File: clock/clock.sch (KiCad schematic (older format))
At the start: 3 parts, among them P101 CONN_01X03, P102 CONN_FAN_PWM, P103 XG4A-1631

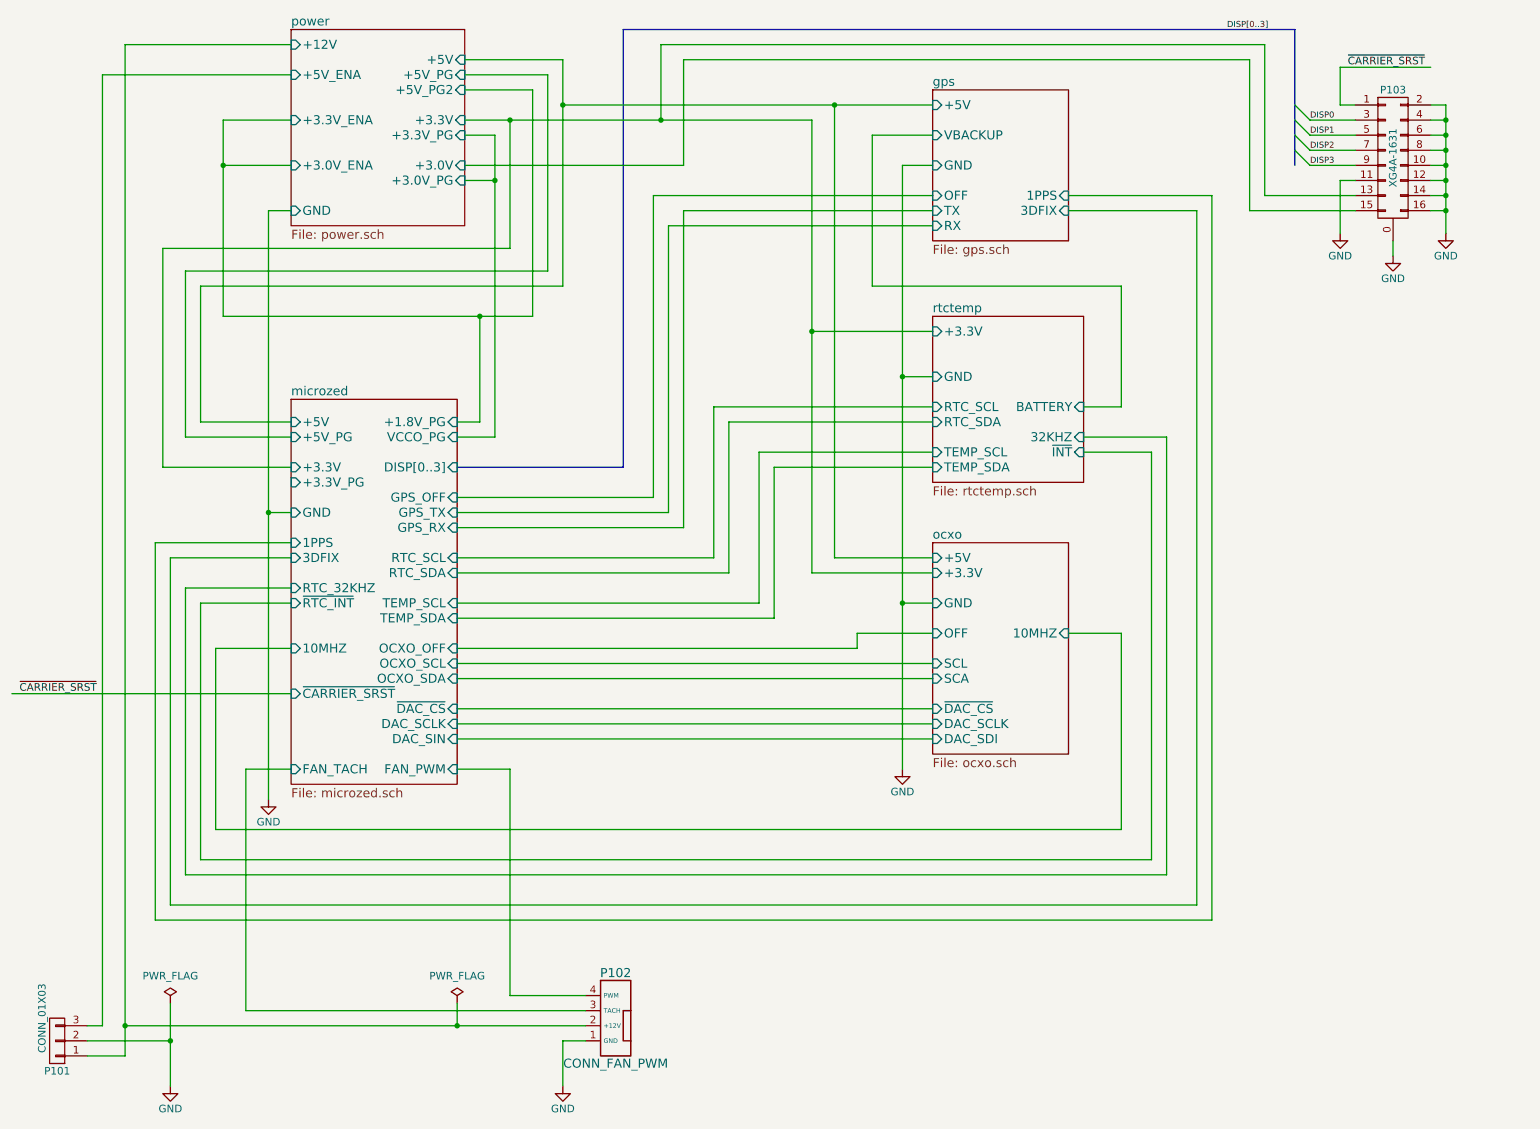
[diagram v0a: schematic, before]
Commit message: Start next revision of the main board. Power sequencing and control changes.
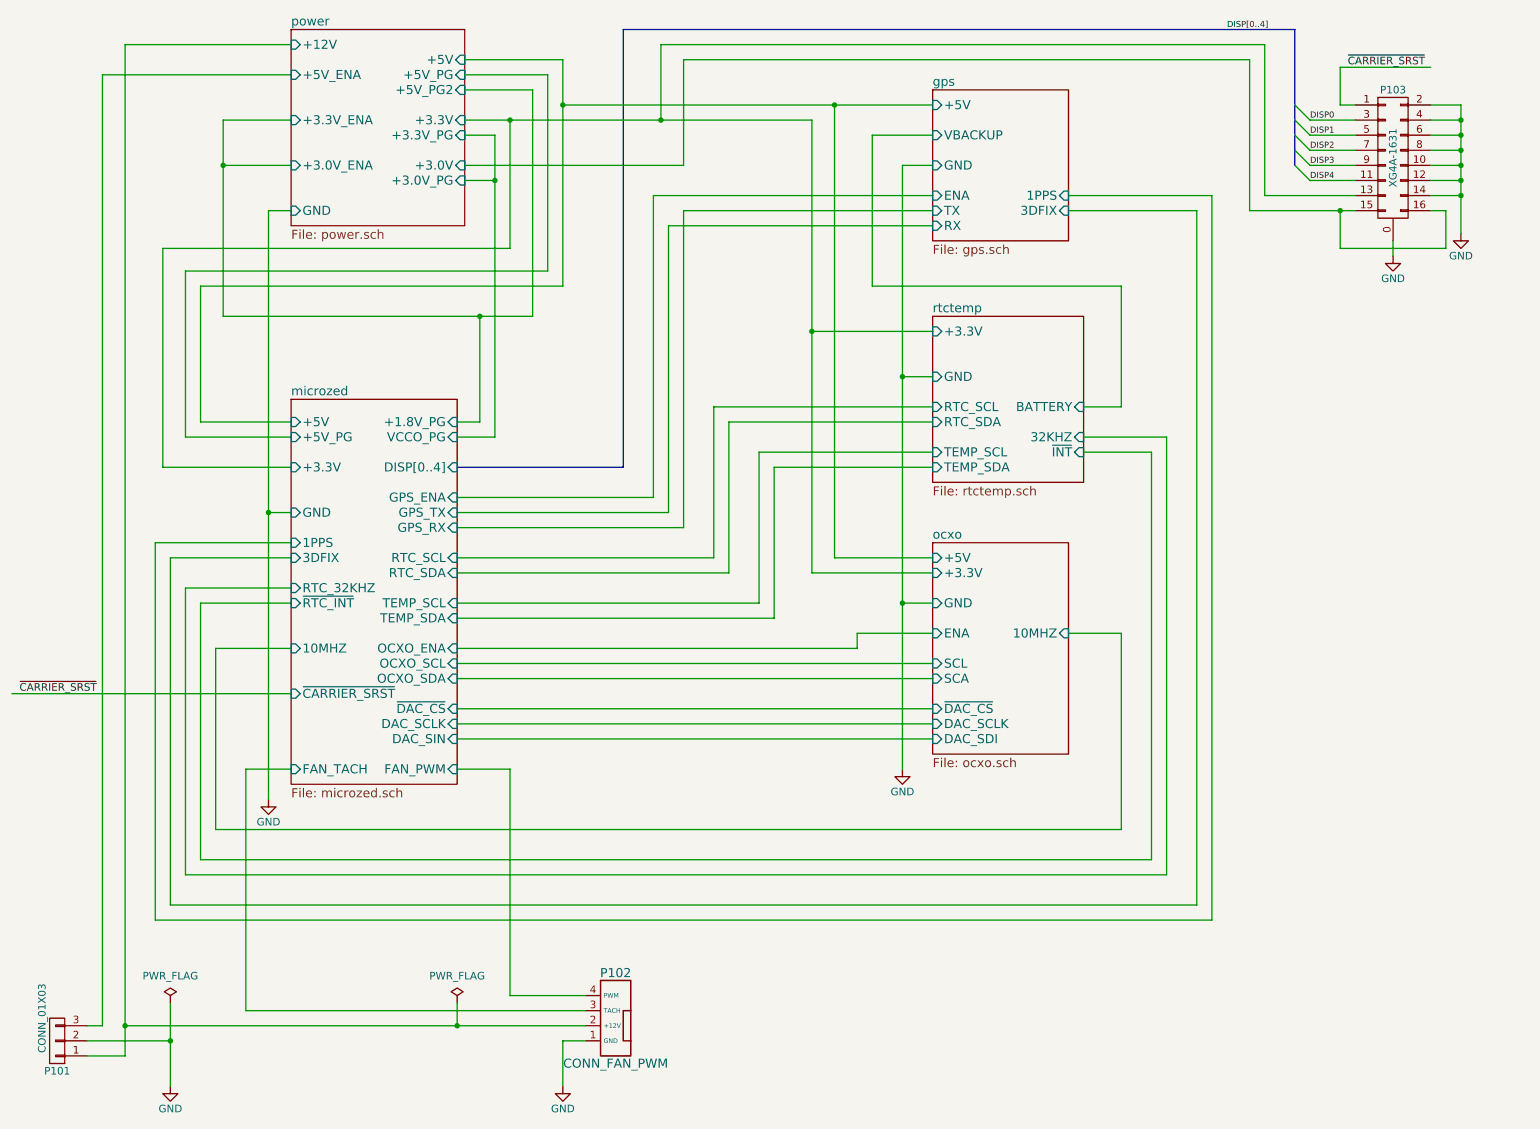
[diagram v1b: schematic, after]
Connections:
- net GND: no longer P103.11 (P11), P103.16 (P16)
- net power/+3.0V: now also P103.16 (P16)
- new net DISP4: P103.11 (P11)
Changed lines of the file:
@@
 F9 "DAC_SDI" I L 6650 5300 60
 F10 "+3.3V" I L 6650 4200 60
-F11 "OFF" I L 6650 4600 60
+F11 "ENA" I L 6650 4600 60
 $EndSheet
 $Sheet
@@
 F7 "VBACKUP" I L 6650 1300 60
 F8 "GND" I L 6650 1500 60
-F9 "OFF" I L 6650 1700 60
+F9 "ENA" I L 6650 1700 60
 $EndSheet
 $Sheet
@@
 F4 "GND" I L 2400 3800 60
 F5 "+5V_PG" I L 2400 3300 60
-F6 "+3.3V_PG" I L 2400 3600 60
-F7 "+1.8V_PG" I R 3500 3200 60
-F8 "VCCO_PG" I R 3500 3300 60
-F9 "GPS_TX" I R 3500 3800 60
-F10 "GPS_RX" I R 3500 3900 60
-F11 "OCXO_SCL" I R 3500 4800 60
-F12 "OCXO_SDA" I R 3500 4900 60
-F13 "~DAC_CS~" I R 3500 5100 60
-F14 "DAC_SCLK" I R 3500 5200 60
-F15 "DAC_SIN" I R 3500 5300 60
-F16 "10MHZ" I L 2400 4700 60
-F17 "1PPS" I L 2400 4000 60
-F18 "3DFIX" I L 2400 4100 60
-F19 "FAN_PWM" I R 3500 5500 60
-F20 "DISP[0..3]" I R 3500 3500 60
-F21 "RTC_SCL" I R 3500 4100 60
-F22 "RTC_SDA" I R 3500 4200 60
-F23 "TEMP_SCL" I R 3500 4400 60
-F24 "TEMP_SDA" I R 3500 4500 60
-F25 "FAN_TACH" I L 2400 5500 60
-F26 "~CARRIER_SRST~" I L 2400 5000 60
-F27 "GPS_OFF" I R 3500 3700 60
-F28 "OCXO_OFF" I R 3500 4700 60
-F29 "RTC_32KHZ" I L 2400 4300 60
-F30 "~RTC_INT~" I L 2400 4400 60
+F6 "+1.8V_PG" I R 3500 3200 60
+F7 "VCCO_PG" I R 3500 3300 60
+F8 "GPS_TX" I R 3500 3800 60
+F9 "GPS_RX" I R 3500 3900 60
+F10 "OCXO_SCL" I R 3500 4800 60
+F11 "OCXO_SDA" I R 3500 4900 60
+F12 "~DAC_CS~" I R 3500 5100 60
+F13 "DAC_SCLK" I R 3500 5200 60
+F14 "DAC_SIN" I R 3500 5300 60
+F15 "10MHZ" I L 2400 4700 60
+F16 "1PPS" I L 2400 4000 60
+F17 "3DFIX" I L 2400 4100 60
+F18 "FAN_PWM" I R 3500 5500 60
+F19 "DISP[0..4]" I R 3500 3500 60
+F20 "RTC_SCL" I R 3500 4100 60
+F21 "RTC_SDA" I R 3500 4200 60
+F22 "TEMP_SCL" I R 3500 4400 60
+F23 "TEMP_SDA" I R 3500 4500 60
+F24 "FAN_TACH" I L 2400 5500 60
+F25 "~CARRIER_SRST~" I L 2400 5000 60
+F26 "GPS_ENA" I R 3500 3700 60
+F27 "OCXO_ENA" I R 3500 4700 60
+F28 "RTC_32KHZ" I L 2400 4300 60
+F29 "~RTC_INT~" I L 2400 4400 60
 $EndSheet
 $Comp
@@
 L GND #PWR03
 U 1 1 5632D32A
-P 10050 1950
-F 0 "#PWR03" H 10050 1700 50  0001 C CNN
-F 1 "GND" H 10050 1800 50  0000 C CNN
-F 2 "" H 10050 1950 60  0000 C CNN
-F 3 "" H 10050 1950 60  0000 C CNN
-	1    10050 1950
-	1    0    0    -1
-$EndComp
-$Comp
-L GND #PWR04
-U 1 1 5632E81A
-P 9350 1950
-F 0 "#PWR04" H 9350 1700 50  0001 C CNN
-F 1 "GND" H 9350 1800 50  0000 C CNN
-F 2 "" H 9350 1950 60  0000 C CNN
-F 3 "" H 9350 1950 60  0000 C CNN
-	1    9350 1950
+P 10150 1950
+F 0 "#PWR03" H 10150 1700 50  0001 C CNN
+F 1 "GND" H 10150 1800 50  0000 C CNN
+F 2 "" H 10150 1950 60  0000 C CNN
+F 3 "" H 10150 1950 60  0000 C CNN
+	1    10150 1950
 	1    0    0    -1
 $EndComp
@@
 DISP3
 Text Label 8600 600  0    40   ~ 0
-DISP[0..3]
+DISP[0..4]
 $Comp
 L CONN_FAN_PWM P102
@@
 	1700 3300 2400 3300
 Wire Wire Line
-	10050 1800 9950 1800
-Connection ~ 10050 1800
-Wire Wire Line
-	10050 1700 9950 1700
-Connection ~ 10050 1700
-Wire Wire Line
-	10050 1600 9950 1600
-Connection ~ 10050 1600
-Wire Wire Line
-	10050 1500 9950 1500
-Connection ~ 10050 1500
-Wire Wire Line
-	10050 1400 9950 1400
-Connection ~ 10050 1400
-Wire Wire Line
-	10050 1300 9950 1300
-Connection ~ 10050 1300
-Wire Wire Line
-	9950 1200 10050 1200
+	10150 1700 9950 1700
+Connection ~ 10150 1700
+Wire Wire Line
+	10150 1600 9950 1600
+Connection ~ 10150 1600
+Wire Wire Line
+	10150 1500 9950 1500
+Connection ~ 10150 1500
+Wire Wire Line
+	10150 1400 9950 1400
+Connection ~ 10150 1400
+Wire Wire Line
+	10150 1300 9950 1300
+Connection ~ 10150 1300
+Wire Wire Line
+	9950 1200 10150 1200
 Wire Wire Line
 	9450 1100 9350 1100
-Wire Wire Line
-	9450 1600 9350 1600
 Wire Wire Line
 	3550 1500 5000 1500
@@
 ~CARRIER_SRST~
 Wire Wire Line
-	10050 1100 10050 1950
+	10150 1100 10150 1950
 Wire Wire Line
 	9350 850  9950 850
@@
 	9350 1100 9350 850
 Wire Wire Line
-	9950 1100 10050 1100
-Connection ~ 10050 1200
-Wire Wire Line
-	9350 1600 9350 1950
+	9950 1100 10150 1100
+Connection ~ 10150 1200
 Wire Wire Line
 	3550 1000 4000 1000
@@
 Wire Wire Line
 	4900 1900 4900 3800
+Entry Wire Line
+	9050 1500 9150 1600
+Wire Wire Line
+	9150 1600 9450 1600
+Text Label 9150 1600 0    40   ~ 0
+DISP4
+Wire Wire Line
+	9950 1800 10050 1800
+Wire Wire Line
+	10050 1800 10050 2050
+Wire Wire Line
+	10050 2050 9350 2050
+Wire Wire Line
+	9350 2050 9350 1800
+Connection ~ 9350 1800
 $EndSCHEMATC

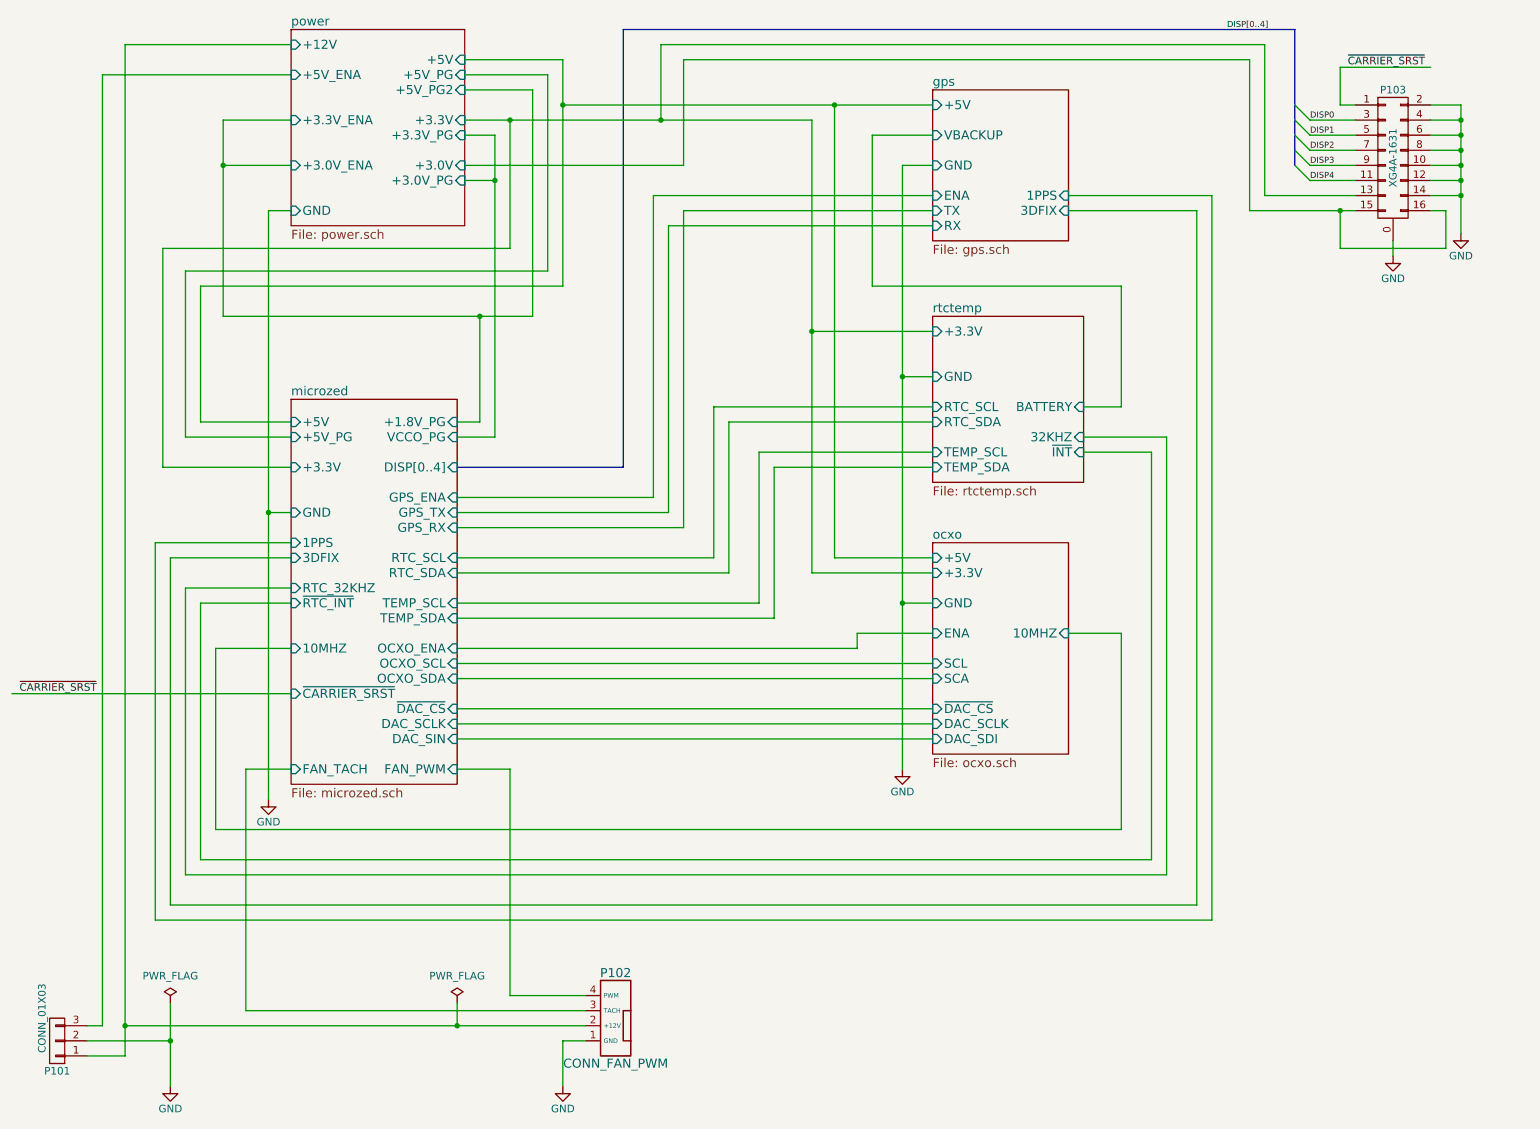
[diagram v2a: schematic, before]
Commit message: Remove sheet to sheet power interconnect because power symbols are global.
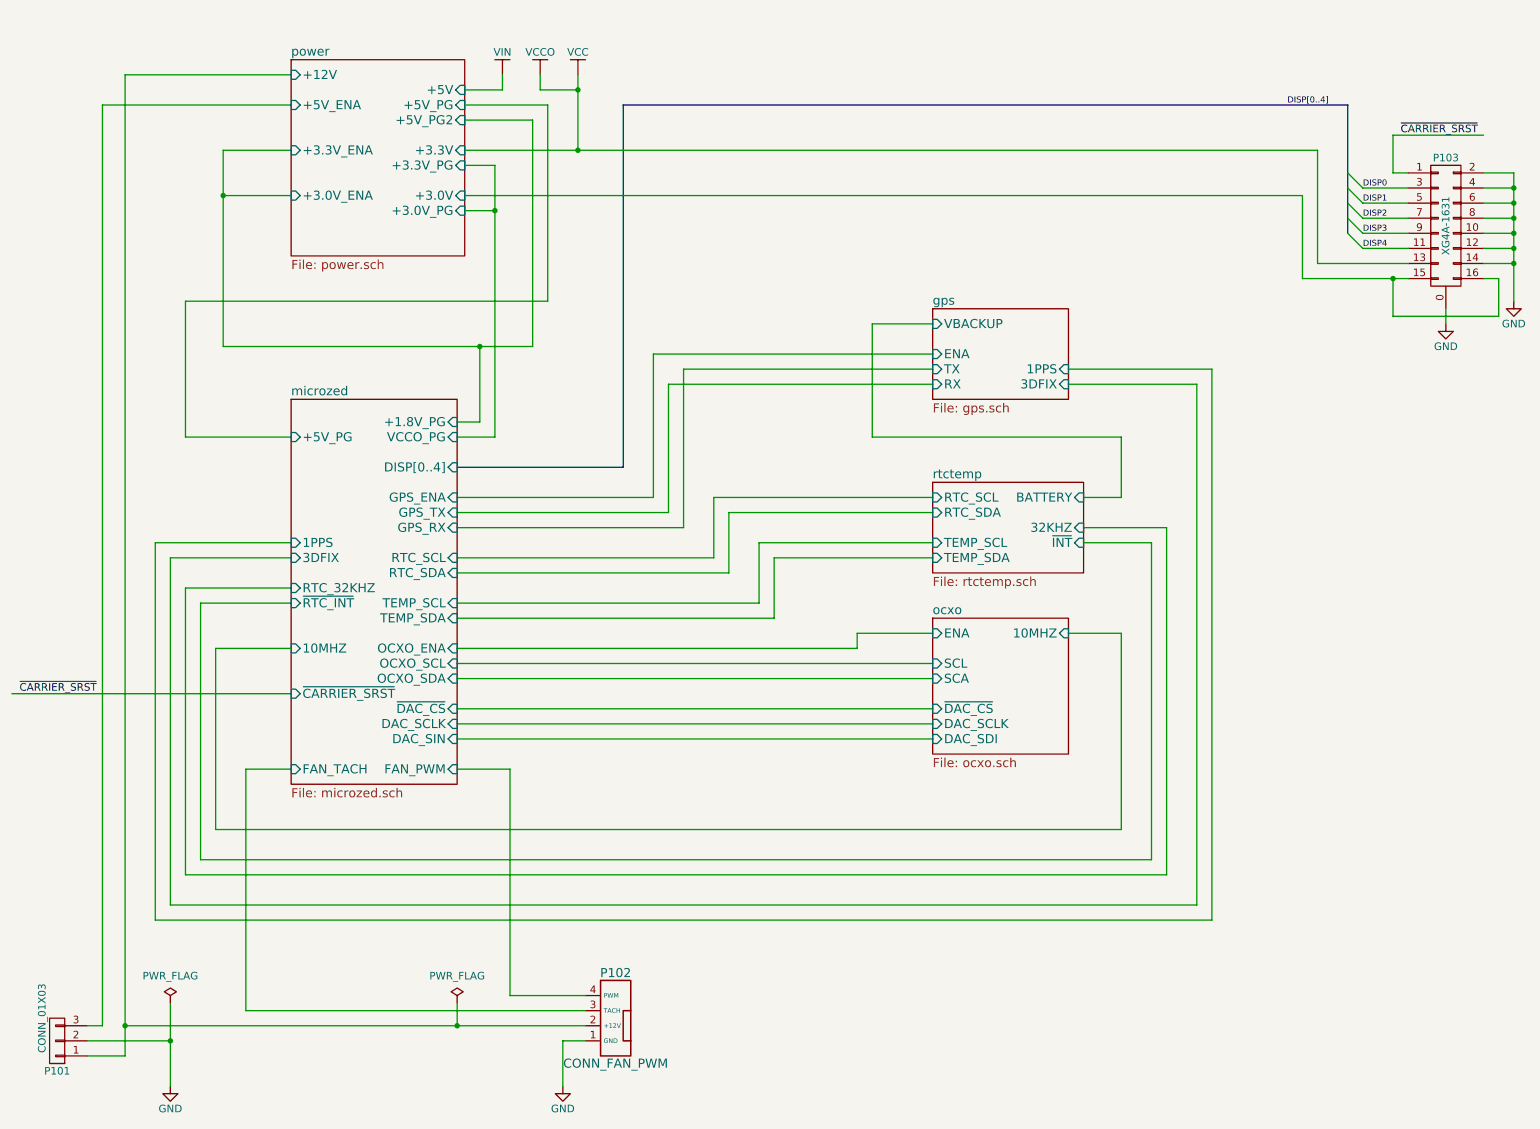
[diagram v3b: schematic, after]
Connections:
- net microzed/+3.3V renamed VCC
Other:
- moved on the sheet: P103

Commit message: Move power indicator LEDs. Clean up test points and silkscreen. Move the gate of Q302 to the other side of R301.
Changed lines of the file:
@@
 	9800 2150 9200 2150
 Wire Wire Line
-	9200 1400 9200 2150
+	9200 2150 9200 1400
 Wire Wire Line
-	3550 1400 9200 1400
+	9200 1400 3550 1400
 Wire Wire Line
 	3500 5100 6650 5100
